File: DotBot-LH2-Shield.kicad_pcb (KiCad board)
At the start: 4 copper layers, 29 x 27 mm, 23 parts, among them J1 Conn_01x04, J2 Conn_01x10, J3 Conn_01x10, Q1 NX6008NBKWX, Q2 NX6008NBKWX, Q3 NX6008NBKWX, U1 ISM330DHCXTR, U2 TS4231, U4 LIS3MDL

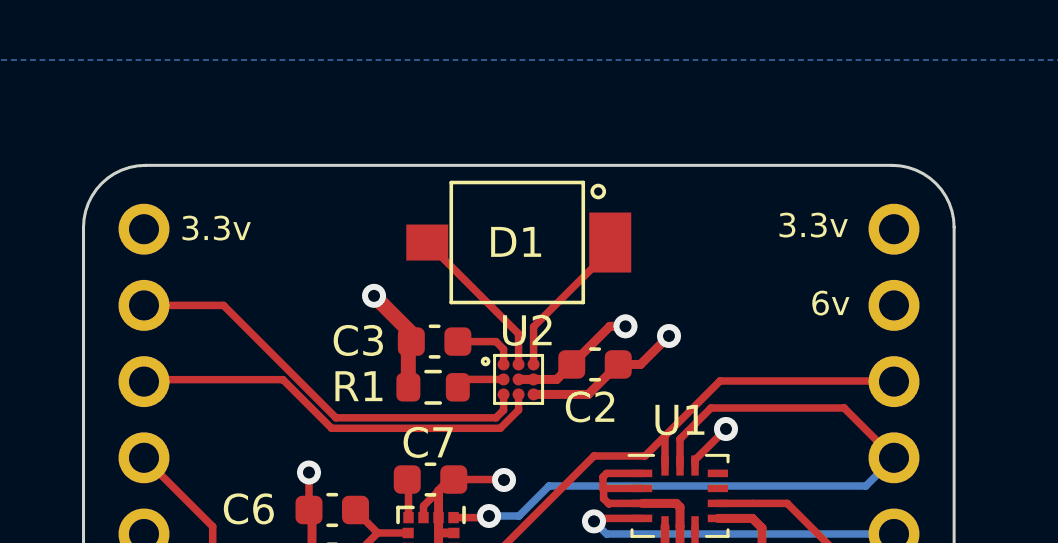
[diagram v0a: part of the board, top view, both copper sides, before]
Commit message: DotBot-LH2-Shield.kicad_pcb: fix 3.3v label on F silkscreen
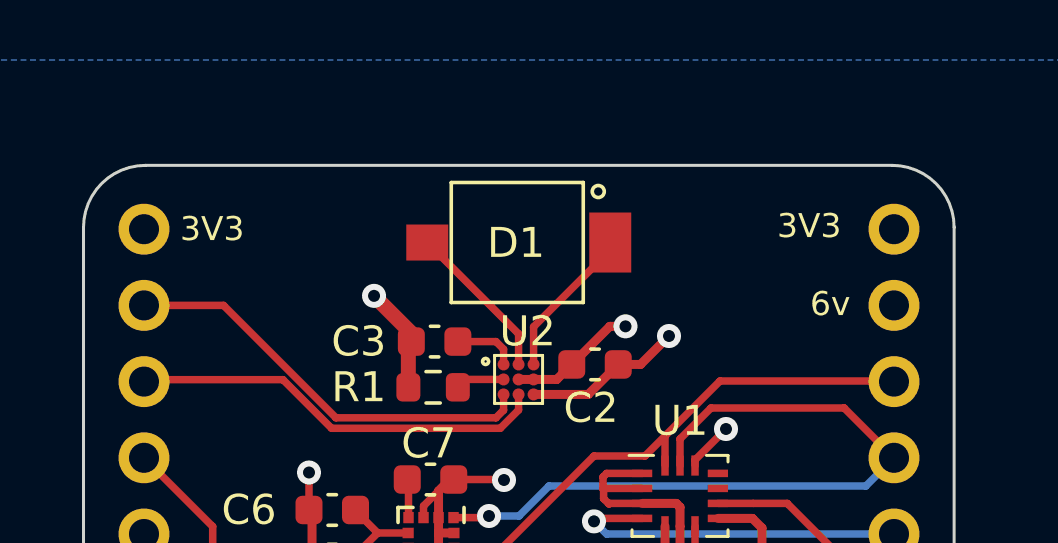
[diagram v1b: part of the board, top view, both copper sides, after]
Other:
- board text removed: "3.3v"
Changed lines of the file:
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@@
     (effects (font (size 0.8 0.8) (thickness 0.1875)) (justify left bottom mirror))
   )
-  (gr_text "3.3v" (at 151.1 100.5) (layer "F.SilkS")
+  (gr_text "3V3" (at 151.1 100.5) (layer "F.SilkS")
     (effects (font (size 0.8 0.8) (thickness 0.15)) (justify left bottom))
   )
@@
     (effects (font (size 0.8 0.8) (thickness 0.15)) (justify left bottom))
   )
-  (gr_text "3.3v" (at 131.2 100.6) (layer "F.SilkS")
+  (gr_text "3V3" (at 131.2 100.6) (layer "F.SilkS")
     (effects (font (size 0.8 0.8) (thickness 0.15)) (justify left bottom))
   )

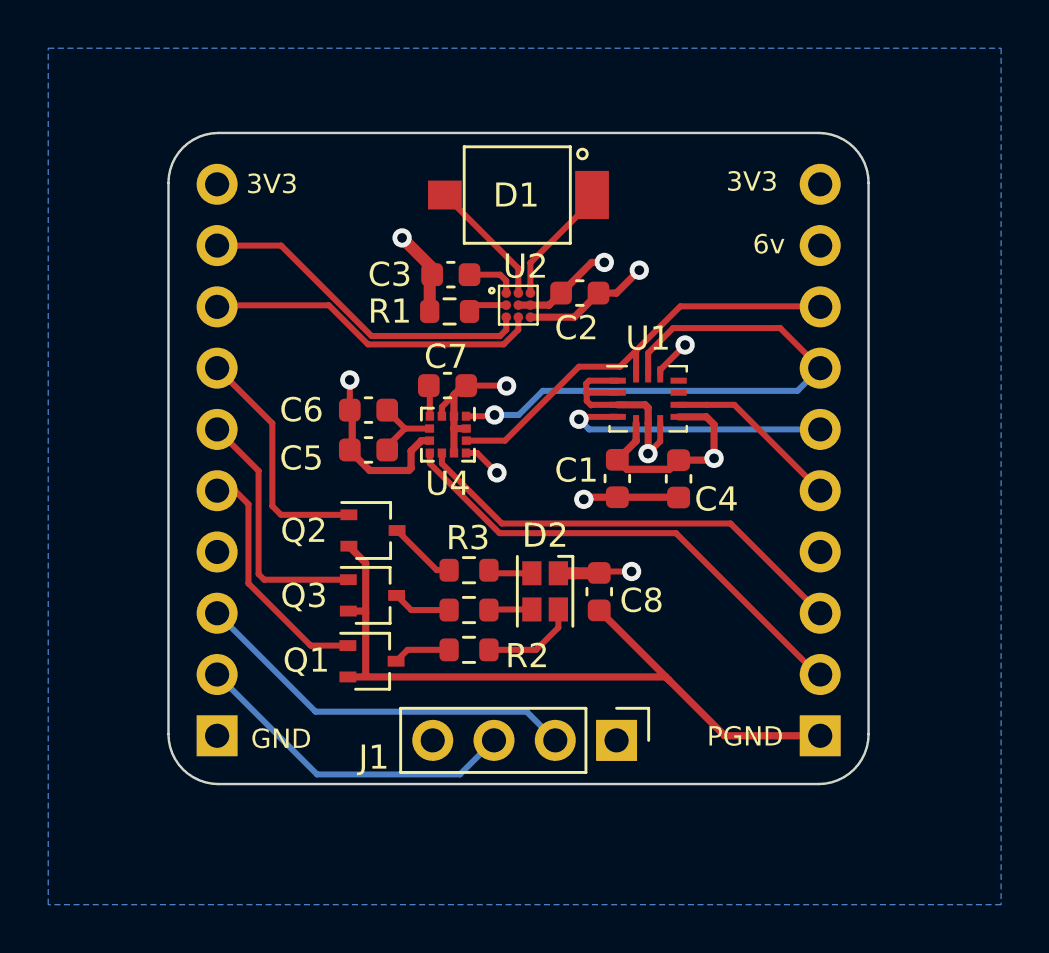
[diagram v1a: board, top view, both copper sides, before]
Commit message: DotBot-LH2-Shield.kicad_pcb: update routing + add stichting vias
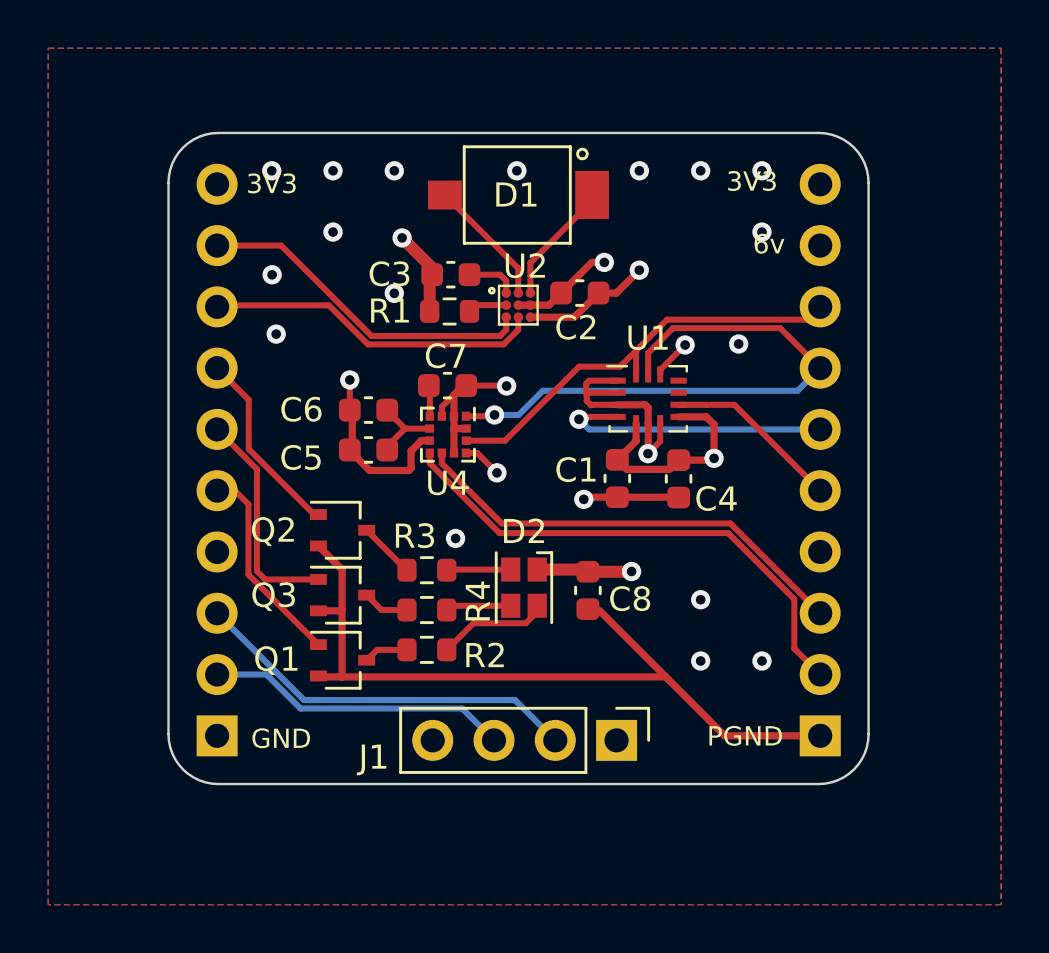
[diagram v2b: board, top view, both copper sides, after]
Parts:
- moved R2 1.75 mm to (138.7, 119.4)
- moved R3 1.75 mm to (138.7, 116.1)
- moved R4 1.75 mm to (138.7, 117.8)
- moved Q2 1.26 mm to (135.2, 114.5)
- moved Q3 1.24 mm to (135.2, 117.2)
- moved Q1 1.22 mm to (135.2, 119.9)
- moved D2 0.89 mm to (142.7, 116.9)
- moved C8 0.47 mm to (145.4, 117.0)
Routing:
- net LED_G: track 9.99 -> 7.91 mm
- net LED_R: track 10.0 -> 8.55 mm
- net LED_B: track 10.5 -> 9.25 mm
- net INT: track 20.2 -> 21.4 mm
- net EXT_1: track 13.8 -> 12.6 mm
- net +6V: track 22.5 -> 23.6 mm
- net GND: track 59.6 -> 60.5 mm, vias 5 -> 22
- net Net-(D2-BK): track 1.79 -> 2.72 mm
- net Net-(D2-GK): track 1.83 -> 2.66 mm
- net Net-(D2-RK): track 4.01 -> 4.65 mm
- net Net-(Q1-D): track 2.39 -> 1.85 mm
- net Net-(Q3-D): track 2.43 -> 1.93 mm
- added copper zone on F.Cu, net GND

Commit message: fix: remove Top ground plane to improve GND separation
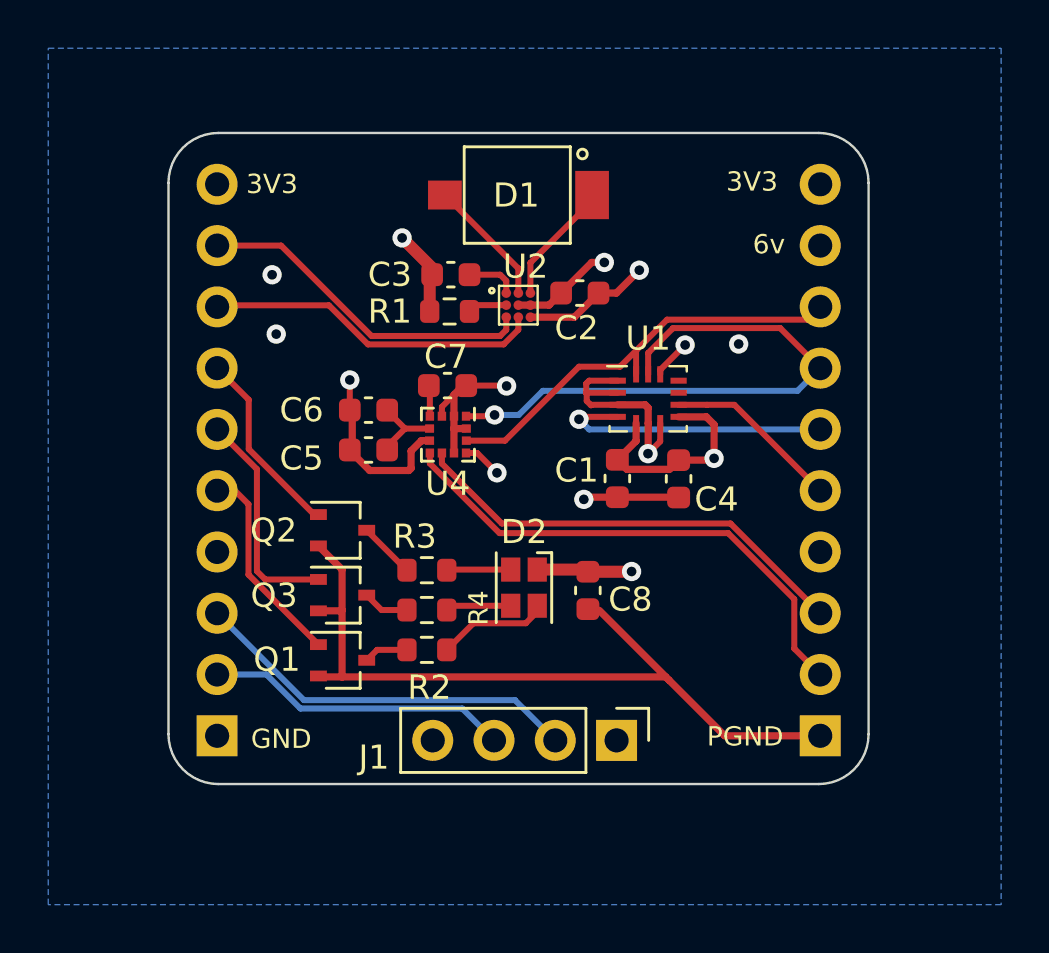
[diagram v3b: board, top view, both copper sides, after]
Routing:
- net GND: vias 22 -> 8
- removed copper zone on F.Cu, net GND
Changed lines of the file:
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@@
     (property "ki_keywords" "R res resistor")
     (attr smd)
-    (fp_text reference "R4" (at 2.145 -0.347 -90) (layer "F.SilkS")
-        (effects (font (size 1 1) (thickness 0.15)))
+    (fp_text reference "R4" (at 2.145 -0.087 270) (layer "F.SilkS")
+        (effects (font (size 0.8 0.8) (thickness 0.15)))
     )
     (fp_text value "750" (at 0 1.43) (layer "F.Fab")
@@
   (footprint "LED_SMD:LED_Cree-PLCC4_2x2mm_CW" (layer "F.Cu")
     (at 142.72 116.86 -90)
-    (descr "2.0mm x 2.0mm PLCC4 LED, https://assets.cree-led.com/a/ds/h/HB-CLMVC-FKA.pdf")
-    (tags "LED Cree PLCC-4 2020 CLMVB-FKA CLMVC-FKA")
+    (descr "2.0mm x 2.0mm PLCC4 LED, http://www.cree.com/~/media/Files/Cree/LED-Components-and-Modules/HB/Data-Sheets/CLMVBFKA.pdf")
+    (tags "LED Cree PLCC-4")
     (property "Link" "https://www.digikey.fr/short/ppj3nqm1")
     (property "Mfr Part Number" "CLMVC-FKA")
@@
     (pad "4" smd rect (at -0.75 0.55 270) (size 1 0.8) (layers "F.Cu" "F.Paste" "F.Mask")
       (net 19 "Net-(D2-GK)") (pinfunction "GK") (pintype "passive"))
-    (model "${KICAD7_3DMODEL_DIR}/LED_SMD.3dshapes/LED_Cree-PLCC4_2x2mm_CW.wrl"
+    (model "${KICAD6_3DMODEL_DIR}/LED_SMD.3dshapes/LED_Cree-PLCC4_2x2mm_CW.wrl"
       (offset (xyz 0 0 0))
       (scale (xyz 1 1 1))
@@
     (property "ki_keywords" "R res resistor")
     (attr smd)
-    (fp_text reference "R2" (at 2.413 0.254) (layer "F.SilkS")
+    (fp_text reference "R2" (at 0.105 1.562) (layer "F.SilkS")
         (effects (font (size 1 1) (thickness 0.15)))
     )
@@
   (segment (start 147.86 111.305) (end 147.8675 111.2975) (width 0.3) (layer "F.Cu") (net 1))
   (segment (start 139.818 110.2405) (end 139.818 109.753) (width 0.3) (layer "F.Cu") (net 1))
-  (via (at 139.884857 114.82) (size 0.8) (drill 0.4) (layers "F.Cu" "B.Cu") (free) (net 1))
-  (via (at 132.264857 99.58) (size 0.8) (drill 0.4) (layers "F.Cu" "B.Cu") (free) (net 1))
-  (via (at 134.804857 102.12) (size 0.8) (drill 0.4) (layers "F.Cu" "B.Cu") (free) (net 1))
-  (via (at 134.804857 99.58) (size 0.8) (drill 0.4) (layers "F.Cu" "B.Cu") (free) (net 1))
-  (via (at 150.044857 117.36) (size 0.8) (drill 0.4) (layers "F.Cu" "B.Cu") (free) (net 1))
   (via (at 146.05 103.378) (size 0.8) (drill 0.4) (layers "F.Cu" "B.Cu") (net 1))
   (via (at 142 108.5) (size 0.8) (drill 0.4) (layers "F.Cu" "B.Cu") (net 1))
@@
   (via (at 151.62 106.76) (size 0.8) (drill 0.4) (layers "F.Cu" "B.Cu") (free) (net 1))
   (via (at 145.2 113.2) (size 0.8) (drill 0.4) (layers "F.Cu" "B.Cu") (net 1))
-  (via (at 147.504857 99.58) (size 0.8) (drill 0.4) (layers "F.Cu" "B.Cu") (free) (net 1))
-  (via (at 150.044857 99.58) (size 0.8) (drill 0.4) (layers "F.Cu" "B.Cu") (free) (net 1))
-  (via (at 152.584857 99.58) (size 0.8) (drill 0.4) (layers "F.Cu" "B.Cu") (free) (net 1))
   (via (at 137.668 102.362) (size 0.8) (drill 0.4) (layers "F.Cu" "B.Cu") (net 1))
-  (via (at 152.584857 102.12) (size 0.8) (drill 0.4) (layers "F.Cu" "B.Cu") (free) (net 1))
   (via (at 147.86 111.305) (size 0.8) (drill 0.4) (layers "F.Cu" "B.Cu") (net 1))
-  (via (at 152.584857 119.9) (size 0.8) (drill 0.4) (layers "F.Cu" "B.Cu") (free) (net 1))
-  (via (at 137.344857 99.58) (size 0.8) (drill 0.4) (layers "F.Cu" "B.Cu") (free) (net 1))
   (via (at 132.28 103.89) (size 0.8) (drill 0.4) (layers "F.Cu" "B.Cu") (free) (net 1))
-  (via (at 142.424857 99.58) (size 0.8) (drill 0.4) (layers "F.Cu" "B.Cu") (free) (net 1))
-  (via (at 137.344857 104.66) (size 0.8) (drill 0.4) (layers "F.Cu" "B.Cu") (free) (net 1))
-  (via (at 150.044857 119.9) (size 0.8) (drill 0.4) (layers "F.Cu" "B.Cu") (free) (net 1))
   (segment (start 146.984 111.9545) (end 148.749 111.9545) (width 0.3) (layer "F.Cu") (net 2))
   (segment (start 140.318 111.278) (end 140.778 111.278) (width 0.25) (layer "F.Cu") (net 2))
@@
   (segment (start 145.28 116.11) (end 145.37 116.2) (width 0.5) (layer "F.Cu") (net 14))
   (segment (start 143.27 116.11) (end 145.28 116.11) (width 0.5) (layer "F.Cu") (net 14))
-  (segment (start 143.423 116.263) (end 143.27 116.11) (width 0.5) (layer "F.Cu") (net 14))
   (segment (start 147.17 116.2) (end 147.18 116.19) (width 0.5) (layer "F.Cu") (net 14))
   (segment (start 145.37 116.2) (end 147.17 116.2) (width 0.5) (layer "F.Cu") (net 14))
@@
     )
   )
-  (zone (net 1) (net_name "GND") (layers "F.Cu" "In1.Cu" "B.Cu") (hatch edge 0.5)
+  (zone (net 1) (net_name "GND") (layers "In1.Cu" "B.Cu") (hatch edge 0.5)
     (connect_pads thru_hole_only (clearance 0.3))
     (min_thickness 0.25) (filled_areas_thickness no)
@@
     )
   )
-  (group "ViaStitching GND" (id 28dbfae4-45da-42f3-acd4-a4e73c88a5df)
-    (members
-      00ffa685-d2c8-42e3-85b7-4fb5c0058256
-      0dcfd7d6-1231-40ea-bc76-3783ee70f4bc
-      12a2e910-01ad-470c-9eb2-4cf24c1f6a76
-      14f0d83f-6688-49a1-a892-b30987db3872
-      1bb7d78c-1256-41dd-af9e-800fc0fe04c5
-      70814dd9-592e-4dae-89c2-6e7fbb0a4995
-      74c0bc1c-c2b5-4ada-a10e-40f85203deda
-      7ce42de5-1976-4fd6-9a61-64f7fcce4651
-      9f274348-3829-43f9-b33c-cceb049b7d3e
-      b68babfa-b772-49f9-a89d-3b913b0fc769
-      b7c45c96-51e3-40e4-8f94-f0f7df3e376b
-      c9b3719b-160e-4e94-b5b2-66b52cd54d5a
-      de1ca234-d43e-4daf-af6c-0be32ea119d0
-      e8a716bb-1d95-470b-8443-13603608e3af
-    )
-  )
